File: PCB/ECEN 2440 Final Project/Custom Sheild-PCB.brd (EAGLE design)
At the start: 58.4 x 102.9 mm, 19 parts

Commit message: final board maybe??
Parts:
- removed RADIOBATTERY: (no value), pinhead:1X02
- added C4, C5: (no value), rcl:PANASONIC_A
- added U$1: BDXXC0A-CBD33C0AWFP-CE2, Custom Library:TO252-5-11
- moved OI_3 49.1 mm to (6.35, 11.4), turned to 0 degrees
- moved OI_2 42.0 mm to (6.35, 17.8), turned to 0 degrees
- moved OI_1 35.8 mm to (6.35, 24.1), turned to 0 degrees
- moved C2 9.25 mm to (31.8, 50.8)
- moved C3 9.25 mm to (38.1, 50.8)
- moved R4 9.25 mm to (27.9, 55.9)
- moved R5 9.25 mm to (34.3, 55.9)
- moved C1 9.25 mm to (25.4, 50.8)
- moved R3 9.25 mm to (22.9, 55.9)
- moved U$4 3.81 mm to (0.00, 57.1)
- moved MAINBATTERY 1.27 mm to (55.9, 11.4), turned to 90 degrees
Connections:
- removed net V+: RADIOBATTERY.2, U$4.VCC
- new net 30: U$3.5V
- net +3V3: now also C5.+, U$1.4
- net GND: now also C4.-, C5.-, U$1.TAB; no longer RADIOBATTERY.1
- net VCC: now also C4.+, U$1.1, U$1.2, U$4.VCC; no longer U$3.5V, U$3.5VA, U$3.5VB
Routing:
- net OI_1: track 21.3 -> 73.4 mm
- net OI_2: track 15.4 -> 61.3 mm
- net +3V3: track 117.6 -> 151.3 mm
- net V+: track 24.0 -> 0.00 mm
- net PD_RADIO: track 52.0 -> 28.0 mm
- net VCC: track 103.5 -> 125.6 mm
- net TX_RADIO: track 34.3 -> 18.1 mm
- net RX_RADIO: track 38.0 -> 21.8 mm
- net OI_3: track 27.8 -> 43.9 mm
- net AUDIO_PTT: track 36.6 -> 50.7 mm
- net AUDIO_PWM: track 14.5 -> 17.8 mm
- net AUDIO_FILTERED: track 13.7 -> 15.3 mm
- net GND: track 0.84 -> 0.00 mm, vias 0 -> 15
- net ALT_SCL: track 38.6 -> 38.7 mm, vias 1 -> 0

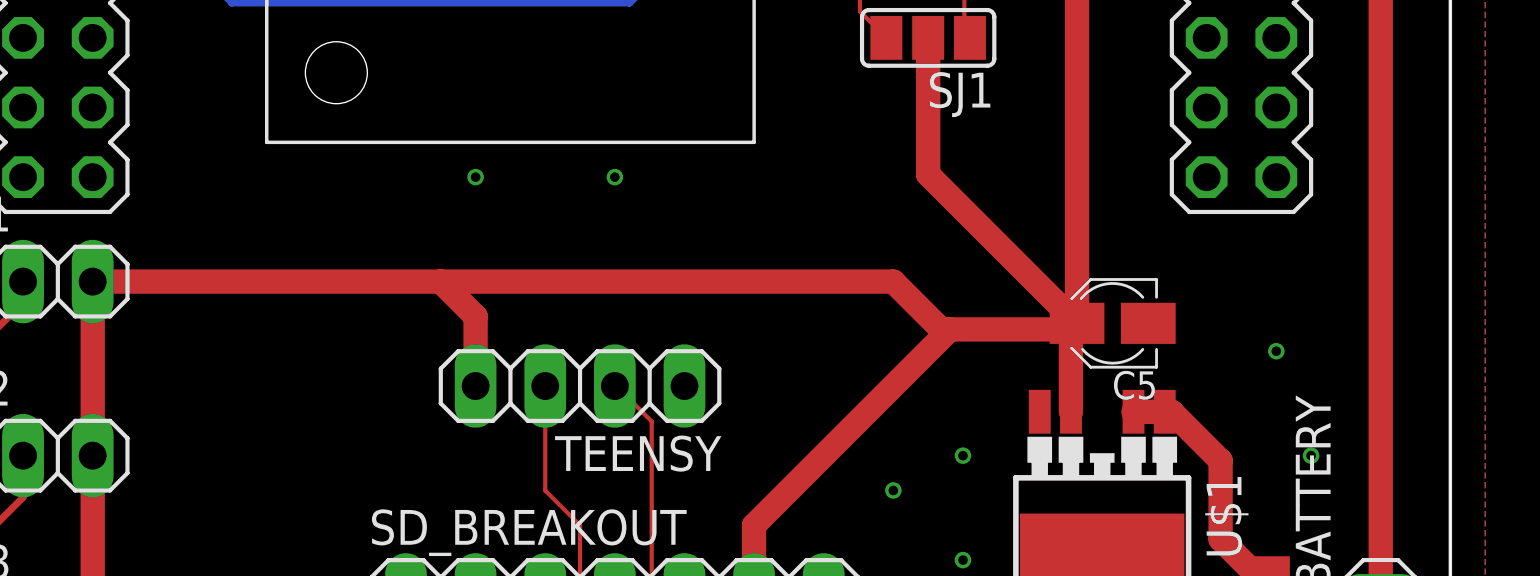
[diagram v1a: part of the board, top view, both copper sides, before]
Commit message: add voltage test points
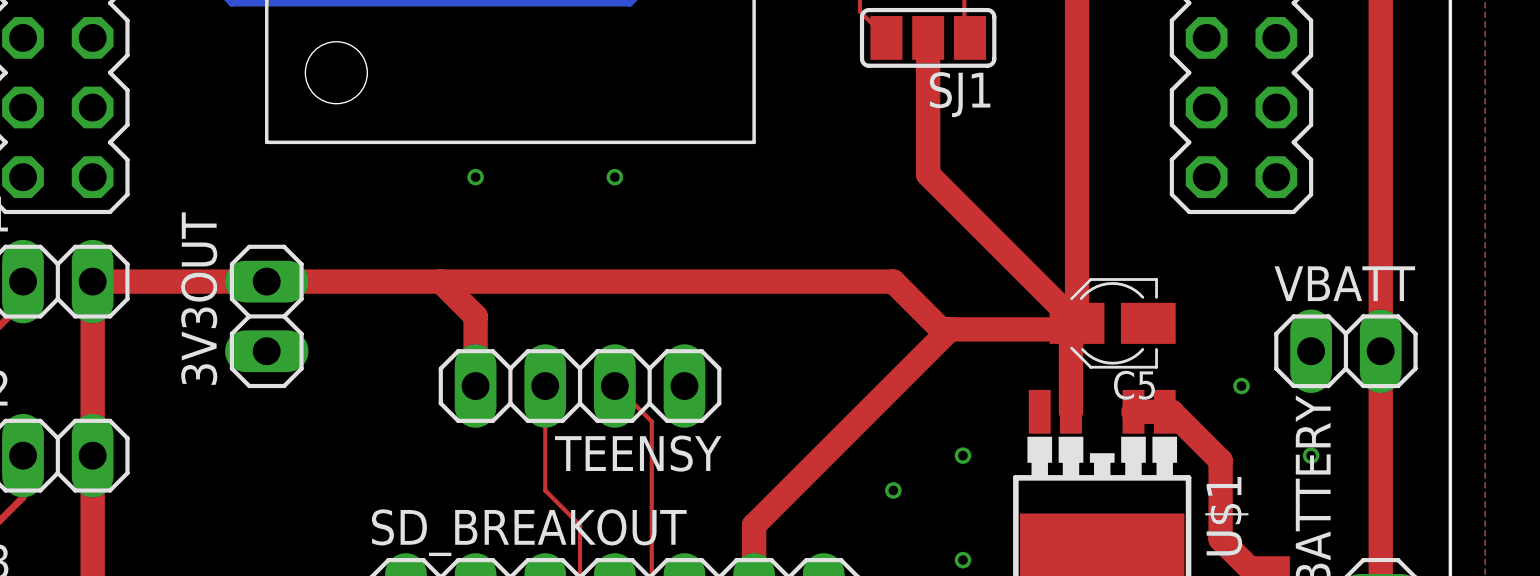
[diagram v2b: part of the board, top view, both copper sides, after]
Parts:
- added 3V3OUT, VBATT: (no value), pinhead:1X02
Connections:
- net +3V3: now also 3V3OUT.2
- net GND: now also 3V3OUT.1, VBATT.1
- net VCC: now also VBATT.2
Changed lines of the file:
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@@
 <attribute name="VALUE" x="47.751" y="25.431" size="1.016" layer="27" rot="R180"/>
+</element>
+<element name="VBATT" library="pinhead" library_urn="urn:adsk.eagle:library:325" package="1X02" package3d_urn="urn:adsk.eagle:package:22435/2" value="" x="54.61" y="21.59" smashed="yes">
+<attribute name="NAME" x="51.9938" y="23.4188" size="1.27" layer="25" ratio="10"/>
+<attribute name="POPULARITY" value="98" x="54.61" y="21.59" size="1.778" layer="27" display="off"/>
+<attribute name="VALUE" x="52.07" y="18.415" size="1.27" layer="27"/>
+</element>
+<element name="3V3OUT" library="pinhead" library_urn="urn:adsk.eagle:library:325" package="1X02" package3d_urn="urn:adsk.eagle:package:22435/2" value="" x="15.24" y="22.86" smashed="yes" rot="R90">
+<attribute name="NAME" x="13.4112" y="20.2438" size="1.27" layer="25" ratio="10" rot="R90"/>
+<attribute name="POPULARITY" value="98" x="15.24" y="22.86" size="1.778" layer="27" rot="R90" display="off"/>
+<attribute name="VALUE" x="18.415" y="20.32" size="1.27" layer="27" rot="R90"/>
 </element>
 </elements>
@@
 <via x="38.1" y="16.51" extent="1-16" drill="0.35"/>
 <via x="53.34" y="17.78" extent="1-16" drill="0.35"/>
-<via x="52.07" y="21.59" extent="1-16" drill="0.35"/>
+<via x="50.8" y="20.32" extent="1-16" drill="0.35"/>
+<contactref element="VBATT" pad="1"/>
+<contactref element="3V3OUT" pad="1"/>
+<wire x1="19.05" y1="74.93" x2="43.18" y2="82.55" width="0" layer="19" extent="1-1"/>
+<wire x1="8.89" y1="72.39" x2="19.05" y2="74.93" width="0" layer="19" extent="1-1"/>
+<wire x1="2.54" y1="90.932" x2="8.89" y2="72.39" width="0" layer="19" extent="1-1"/>
+<wire x1="6.35" y1="50.8" x2="8.89" y2="72.39" width="0" layer="19" extent="1-1"/>
+<wire x1="21.59" y1="48.26" x2="6.35" y2="50.8" width="0" layer="19" extent="1-1"/>
+<wire x1="25.4" y1="49.85" x2="21.59" y2="48.26" width="0" layer="19" extent="1-1"/>
+<wire x1="29.21" y1="48.26" x2="25.4" y2="49.85" width="0" layer="19" extent="1-1"/>
+<wire x1="31.75" y1="49.85" x2="29.21" y2="48.26" width="0" layer="19" extent="1-1"/>
+<wire x1="38.1" y1="49.85" x2="31.75" y2="49.85" width="0" layer="19" extent="1-1"/>
+<wire x1="38.1" y1="45.72" x2="38.1" y2="49.85" width="0" layer="19" extent="1-1"/>
+<wire x1="38.862" y1="35.306" x2="38.1" y2="45.72" width="0" layer="19" extent="1-1"/>
+<wire x1="49.53" y1="48.26" x2="38.1" y2="49.85" width="0" layer="19" extent="1-1"/>
+<wire x1="17.78" y1="36.83" x2="21.59" y2="48.26" width="0" layer="19" extent="1-1"/>
+<wire x1="22.86" y1="27.94" x2="17.78" y2="36.83" width="0" layer="19" extent="1-1"/>
+<wire x1="27.94" y1="27.94" x2="22.86" y2="27.94" width="0" layer="19" extent="1-1"/>
+<wire x1="30.48" y1="20.32" x2="27.94" y2="27.94" width="0" layer="19" extent="1-1"/>
+<wire x1="38.1" y1="16.51" x2="30.48" y2="20.32" width="0" layer="19" extent="1-1"/>
+<wire x1="40.64" y1="17.78" x2="38.1" y2="16.51" width="0" layer="19" extent="1-1"/>
+<wire x1="40.64" y1="13.97" x2="38.1" y2="16.51" width="0" layer="19" extent="1-1"/>
+<wire x1="35.56" y1="12.7" x2="38.1" y2="16.51" width="0" layer="19" extent="1-1"/>
+<wire x1="45.72" y1="12.67" x2="40.64" y2="13.97" width="0" layer="19" extent="1-1"/>
+<wire x1="51.816" y1="10.511" x2="45.72" y2="12.67" width="0" layer="19" extent="1-1"/>
+<wire x1="55.88" y1="10.16" x2="51.816" y2="10.511" width="0" layer="19" extent="1-1"/>
+<wire x1="53.34" y1="17.78" x2="51.816" y2="10.511" width="0" layer="19" extent="1-1"/>
+<wire x1="50.8" y1="20.32" x2="53.34" y2="17.78" width="0" layer="19" extent="1-1"/>
+<wire x1="47.401" y1="22.606" x2="50.8" y2="20.32" width="0" layer="19" extent="1-1"/>
+<wire x1="55.88" y1="2.54" x2="55.88" y2="10.16" width="0" layer="19" extent="1-1"/>
+<wire x1="3.81" y1="24.13" x2="17.78" y2="36.83" width="0" layer="19" extent="1-1"/>
+<wire x1="3.81" y1="17.78" x2="3.81" y2="24.13" width="0" layer="19" extent="1-1"/>
+<wire x1="3.81" y1="11.43" x2="3.81" y2="17.78" width="0" layer="19" extent="1-1"/>
+<wire x1="6.35" y1="7.62" x2="3.81" y2="11.43" width="0" layer="19" extent="1-1"/>
+<wire x1="6.35" y1="5.08" x2="6.35" y2="7.62" width="0" layer="19" extent="1-1"/>
+<wire x1="53.34" y1="21.59" x2="6.35" y2="5.08" width="0" layer="19" extent="1-1"/>
+<wire x1="15.24" y1="21.59" x2="53.34" y2="21.59" width="0" layer="19" extent="1-1"/>
 </signal>
 <signal name="ALT_SDA">
@@
 <wire x1="46.99" y1="54.61" x2="41.656" y2="49.276" width="0.889" layer="1"/>
 <wire x1="41.656" y1="49.276" x2="41.656" y2="40.386" width="0.889" layer="1"/>
+<contactref element="3V3OUT" pad="2"/>
+<wire x1="15.24" y1="24.13" x2="8.89" y2="11.43" width="0" layer="19" extent="1-1"/>
 </signal>
 <signal name="SD_CD1">
@@
 <wire x1="48" y1="19.38" x2="48.254" y2="19.38" width="0.889" layer="1"/>
 <wire x1="50.038" y1="17.596" x2="50.038" y2="14.732" width="0.889" layer="1"/>
+<contactref element="VBATT" pad="2"/>
+<wire x1="55.88" y1="21.59" x2="46.86" y2="19.38" width="0" layer="19" extent="1-1"/>
 </signal>
 <signal name="N$1">

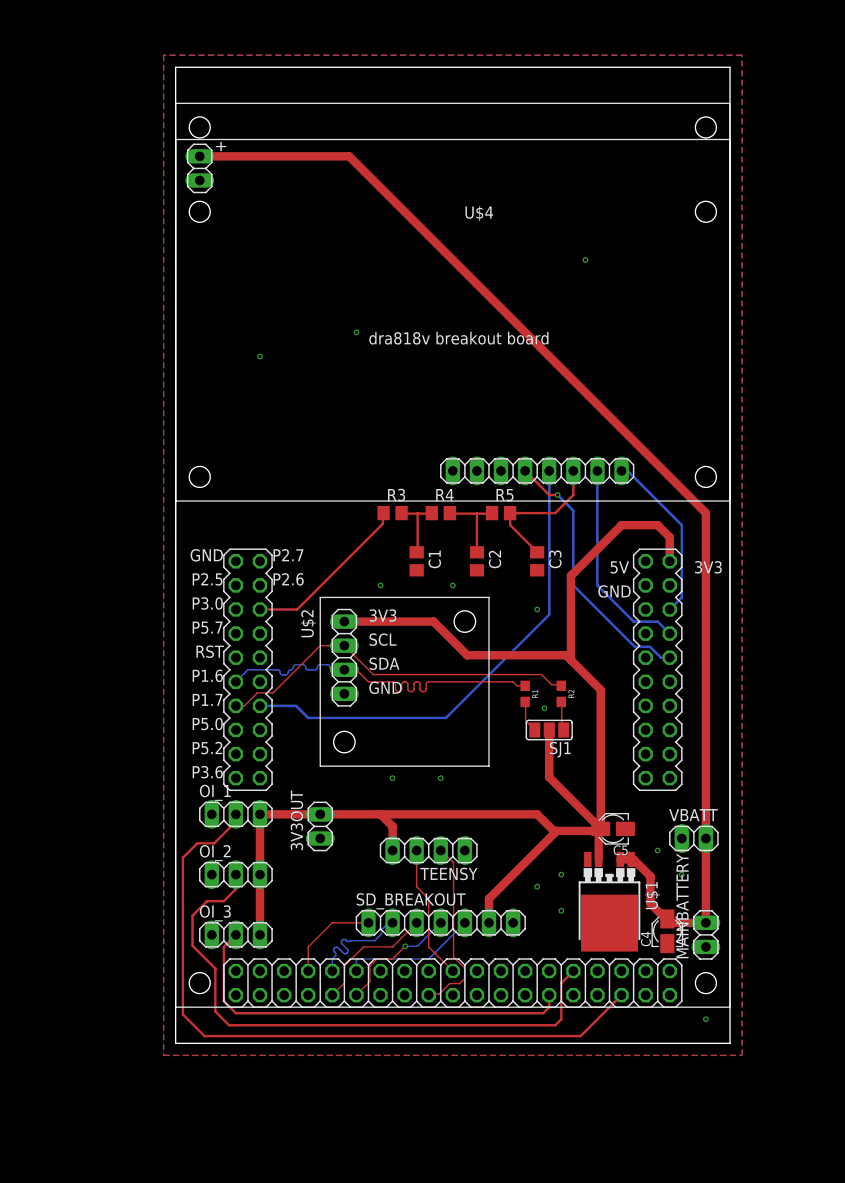
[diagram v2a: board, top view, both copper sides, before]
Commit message: Fix MSP432 footprint
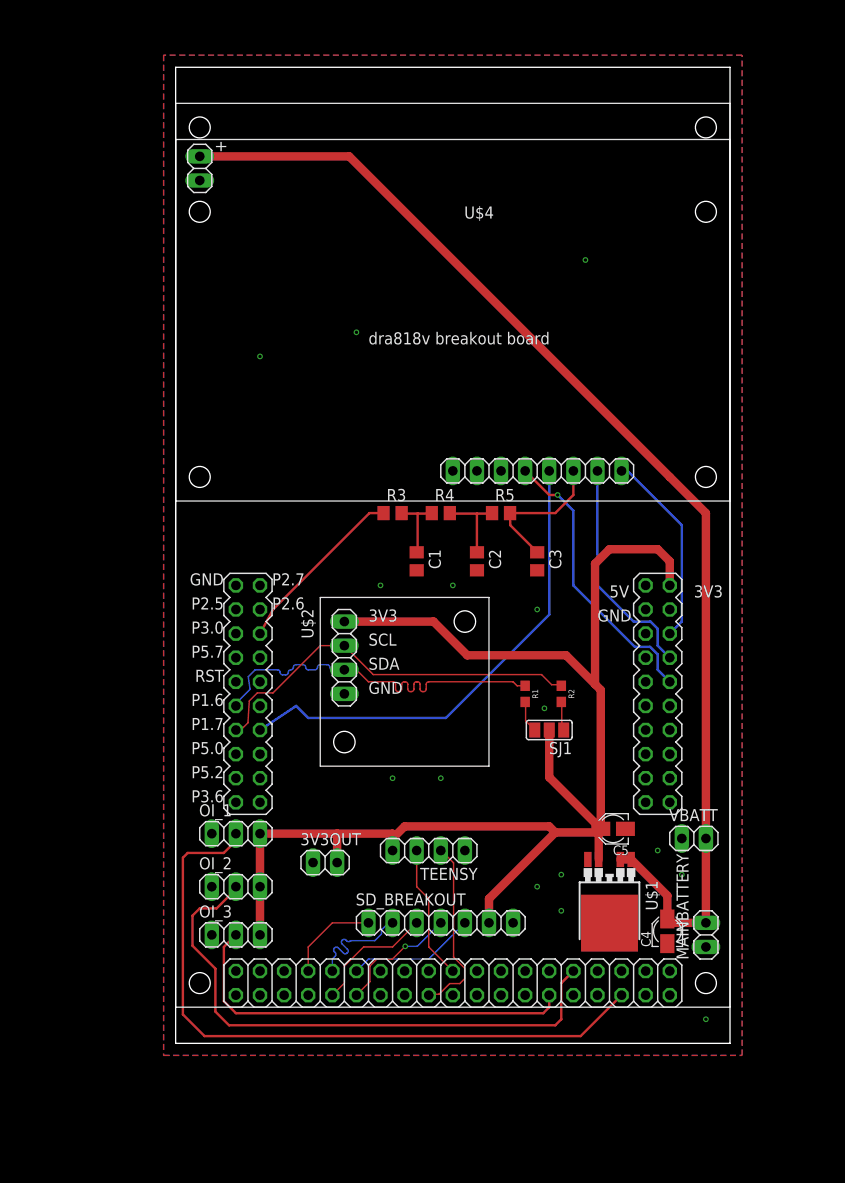
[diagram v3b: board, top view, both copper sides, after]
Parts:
- moved 3V3OUT 3.84 mm to (15.7, 19.1), turned to 0 degrees
- moved OI_1 2.03 mm to (6.35, 22.1)
- moved OI_2 1.27 mm to (6.35, 16.5)
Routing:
- net TX_RADIO: track 18.1 -> 20.7 mm
- net ALT_SCL: track 38.7 -> 40.9 mm
- net ALT_SDA: track 37.3 -> 39.5 mm
- net RX_RADIO: track 21.8 -> 23.9 mm
- net PD_RADIO: track 28.0 -> 30.0 mm
- net OI_2: track 61.3 -> 60.0 mm
- net AUDIO_PWM: track 17.8 -> 18.7 mm
- net OI_1: track 73.4 -> 72.6 mm
- net AUDIO_PTT: track 50.7 -> 51.4 mm
- net SD_CS_SPI: track 14.3 -> 13.5 mm

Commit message: really important commit
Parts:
- added U$5: MEOWTH, Custom Library:MEOWTH
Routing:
- net VCC: track 125.3 -> 131.3 mm
- net AUDIO_PTT: track 51.4 -> 50.5 mm
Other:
- board size 58.4 x 102.9 mm -> 58.4 x 100 mm
- board text added: "+"
- board text added: "-"
- board text added: "T E A M R O C K E T ecen 2440 fall 2019 final project XuTao Ho | Dustin Horn | Giselle Koo"
- board text added: "rx"
- board text added: "tx"

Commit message: final board stuff
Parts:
- C4, C5: value (none) -> 1u
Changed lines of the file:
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@@
 <attribute name="VALUE" x="40.64" y="17.145" size="1.27" layer="27" rot="R270"/>
 </element>
-<element name="C4" library="rcl" library_urn="urn:adsk.eagle:library:334" package="PANASONIC_A" package3d_urn="urn:adsk.eagle:package:23418/2" value="" x="51.816" y="11.811" smashed="yes" rot="R90">
+<element name="C4" library="rcl" library_urn="urn:adsk.eagle:library:334" package="PANASONIC_A" package3d_urn="urn:adsk.eagle:package:23418/2" value="1u" x="51.816" y="11.811" smashed="yes" rot="R90">
 <attribute name="NAME" x="50.066" y="10.161" size="1.016" layer="25" rot="R90"/>
 <attribute name="POPULARITY" value="1" x="51.816" y="11.811" size="1.778" layer="27" rot="R90" display="off"/>
@@
 <attribute name="VALUE" x="54.641" y="10.161" size="1.016" layer="27" rot="R90"/>
 </element>
-<element name="C5" library="rcl" library_urn="urn:adsk.eagle:library:334" package="PANASONIC_A" package3d_urn="urn:adsk.eagle:package:23418/2" value="" x="46.101" y="22.606" smashed="yes" rot="R180">
+<element name="C5" library="rcl" library_urn="urn:adsk.eagle:library:334" package="PANASONIC_A" package3d_urn="urn:adsk.eagle:package:23418/2" value="1u" x="46.101" y="22.606" smashed="yes" rot="R180">
 <attribute name="NAME" x="47.751" y="20.856" size="1.016" layer="25" rot="R180"/>
 <attribute name="POPULARITY" value="1" x="46.101" y="22.606" size="1.778" layer="27" rot="R180" display="off"/>
